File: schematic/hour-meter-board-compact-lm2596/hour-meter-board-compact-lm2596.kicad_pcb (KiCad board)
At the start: 2 copper layers, 80 x 80 mm, 126 parts, among them J101 VIN 9-36V, J201 USB-C, J301 VEHICLE IN, J501 WP, J701 RS485, J702 TERM, J703 BIAS, J801 UART, J802 GPS, J803 QWIIC, J804 EXP, Q201 MMBT3904, Q202 MMBT3904, SW201 RESET, SW202 BOOT, U101 LM2596S-ADJ, U201 ESP32-WROOM-32E-N4, U202 CH340C, U203 USBLC6-2SC6, U204 AMS1117-3.3, U301 PC817C-S, U302 PC817C-S, U401 DS3231MZ+TRL, U501 AT24C256 DIP-8 (socketed), U601 MPU-6500, U602 LIS3MDLTR, U701 THVD2410DR, U801 74LVC1G17GW, U802 SRV05-4

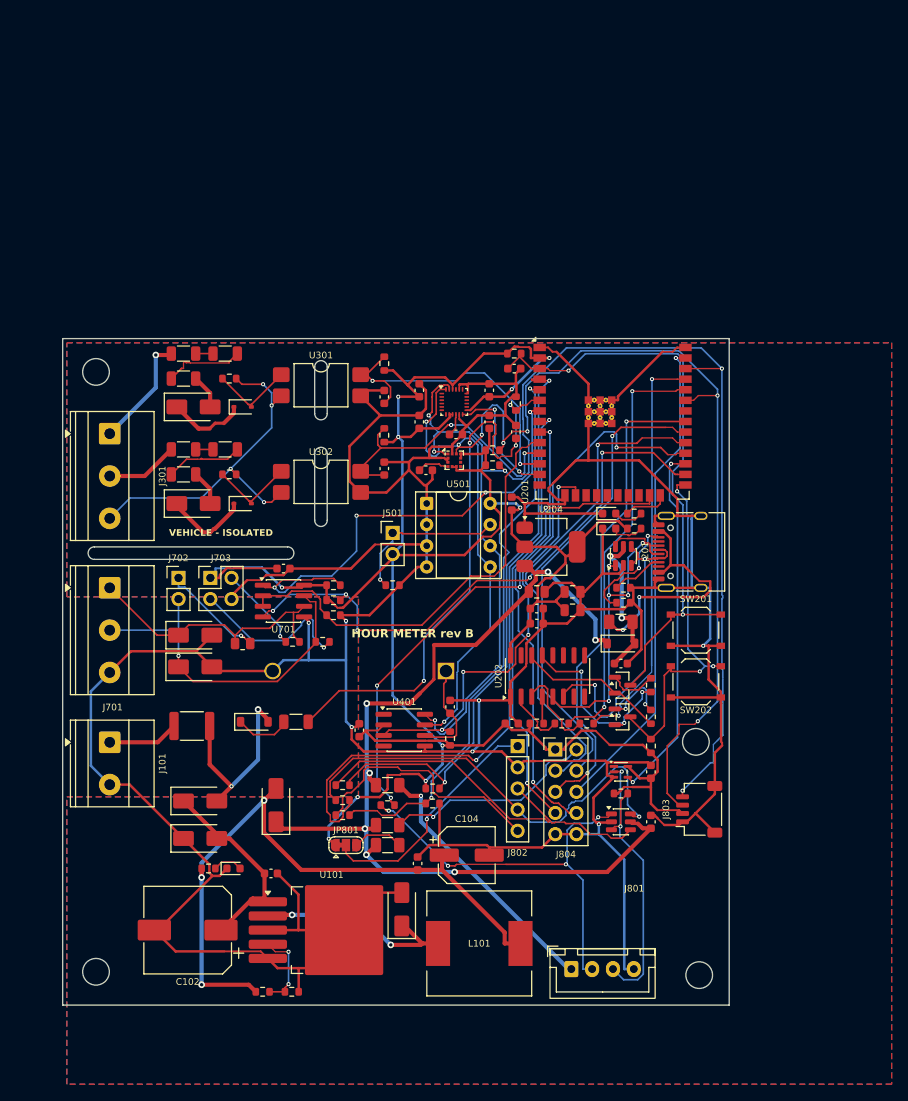
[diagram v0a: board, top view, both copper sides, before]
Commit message: feat(pcb): use JST VH field connectors on the LM2596 compact board
- J101 (VIN 9-30V), J301 (vehicle IN), J701 (RS485) and J801 (UART) are
  latching JST VH headers instead of screw terminals and JST XH
- add TP101 VIN solder pads in parallel with J101
- GPS J802 becomes a 1x5 male pin header
- re-route the board (U203 VBUS escape fixed by re-routing the USB and
  ESP32 lines under it) and regenerate the JLCPCB order files
- tools-pcb.py: `models` command fetches the JLCPCB/EasyEDA STEP models;
  the downloaded 3d/ folders are git-ignored
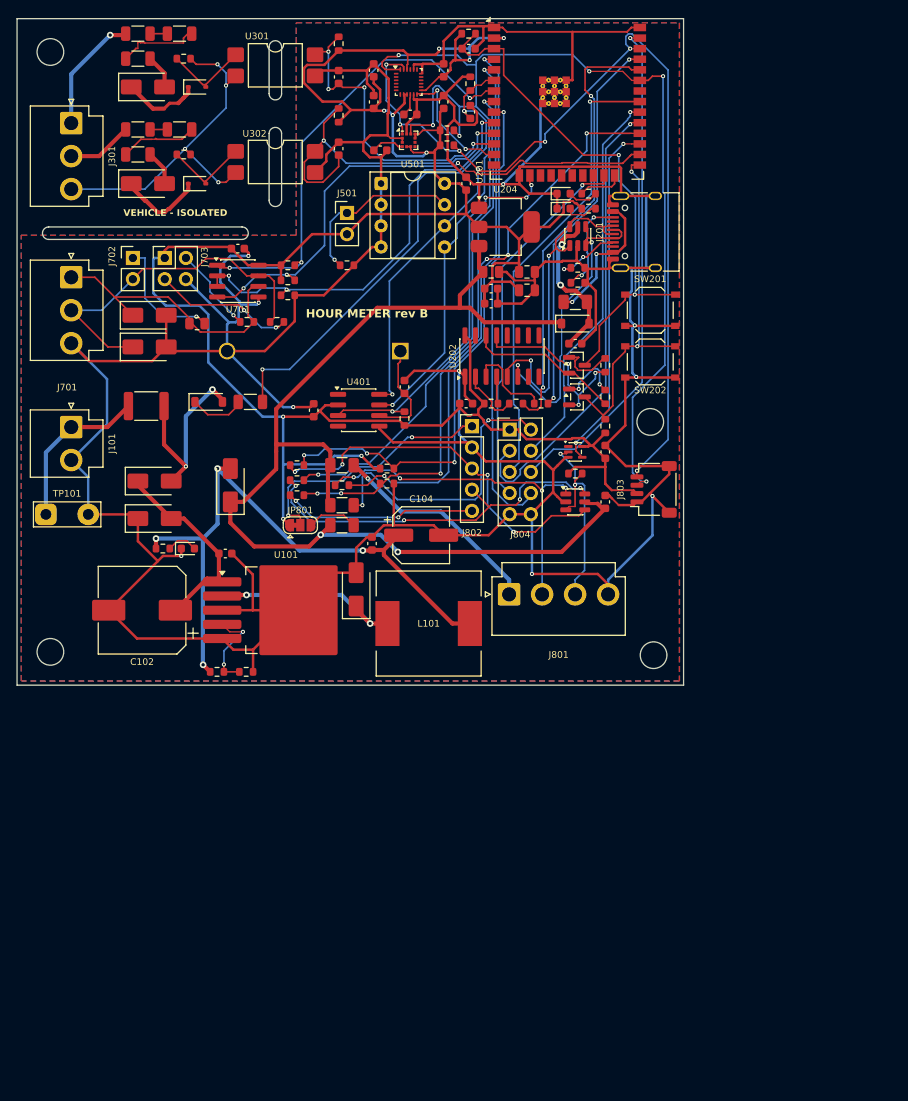
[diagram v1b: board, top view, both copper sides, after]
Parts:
- added TP101: VIN pads, TestPoint:TestPoint_2Pads_Pitch5.08mm_Drill1.3mm, F.Cu at (98.0, 121.1)
- J101: value VIN 9-36V -> VIN 9-30V; footprint TerminalBlock_Phoenix:TerminalBlock_Phoenix_MKDS-1,5-2-5.08_1x02_P5.08mm_Horizontal -> Connector_JST:JST_VH_B2P-VH_1x02_P3.96mm_Vertical
- J301, J701: footprint TerminalBlock_Phoenix:TerminalBlock_Phoenix_MKDS-1,5-3-5.08_1x03_P5.08mm_Horizontal -> Connector_JST:JST_VH_B3P-VH_1x03_P3.96mm_Vertical
- J801: footprint Connector_JST:JST_XH_B4B-XH-A_1x04_P2.50mm_Vertical -> Connector_JST:JST_VH_B4P-VH_1x04_P3.96mm_Vertical
- J802: footprint Connector_PinSocket_2.54mm:PinSocket_1x05_P2.54mm_Vertical -> Connector_PinHeader_2.54mm:PinHeader_1x05_P2.54mm_Vertical
- moved J801 45.6 mm to (153.6, 130.7)
- moved L101 38.9 mm to (143.9, 134.2)
- moved C601 38.8 mm to (137.3, 67.8)
- moved C604 38.8 mm to (137.3, 71.6)
- moved H103 38.8 mm to (170.5, 110.0)
- moved R207 38.8 mm to (161.8, 91.5)
- moved BT401 38.8 mm to (140.5, 101.5)
- moved C101 38.8 mm to (148.9, 72.8)
- moved C102 38.8 mm to (109.5, 132.6)
- moved C104 38.8 mm to (143.0, 123.6)
- moved C105 38.8 mm to (137.1, 124.6)
- moved C201 38.8 mm to (155.7, 92.0)
- moved C202 38.8 mm to (151.4, 94.0)
- moved C205 38.8 mm to (151.4, 92.0)
- moved C208 38.8 mm to (161.5, 100.6)
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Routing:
- net /I2C_SCL: track 163.8 -> 142.6 mm, vias 6 -> 8
- net /GPS_RXD: track 74.3 -> 59.8 mm
- net +5V: track 119.9 -> 133.4 mm, vias 7 -> 2
- net /ESP32 core + USB (DevKitC)/VBUS_IN: track 29.1 -> 17.0 mm
- net Net-(J101-Pin_1): track 8.53 -> 19.6 mm
- net /Ports (UART, GPS, Qwiic, expansion)/UART_RXD_EXT: track 36.6 -> 25.9 mm
- net /ESP32 core + USB (DevKitC)/ESP_EN: track 73.5 -> 63.1 mm
- net /VIN_SENSE: track 69.4 -> 59.7 mm, vias 4 -> 2
- net /EXP_IO18: track 56.5 -> 46.8 mm
- net /Ports (UART, GPS, Qwiic, expansion)/EXP_5V: track 25.9 -> 35.2 mm, vias 1 -> 2
- net /EXP_IO15: track 54.1 -> 45.4 mm, vias 2 -> 1
- net /Ports (UART, GPS, Qwiic, expansion)/GPS_RX_EXT: track 53.4 -> 45.9 mm, vias 1 -> 4
- net /Ports (UART, GPS, Qwiic, expansion)/UART_TXD_EXT: track 50.1 -> 43.2 mm
- net /Ports (UART, GPS, Qwiic, expansion)/GPS_PPS_EXT: track 30.0 -> 23.2 mm, vias 0 -> 2
- net /I2C_SDA: track 165.4 -> 159.4 mm, vias 8 -> 7
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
